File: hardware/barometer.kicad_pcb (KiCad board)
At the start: 2 copper layers, 15 x 25 mm, 24 parts, among them P1 CON-SENSOR2, P2 CONN_01X01, P3 BOOT, U1 XMC1XXX24, U2 LPS22HB, U3 DRILL, U4 DRILL, U5 DRILL, U6 DRILL

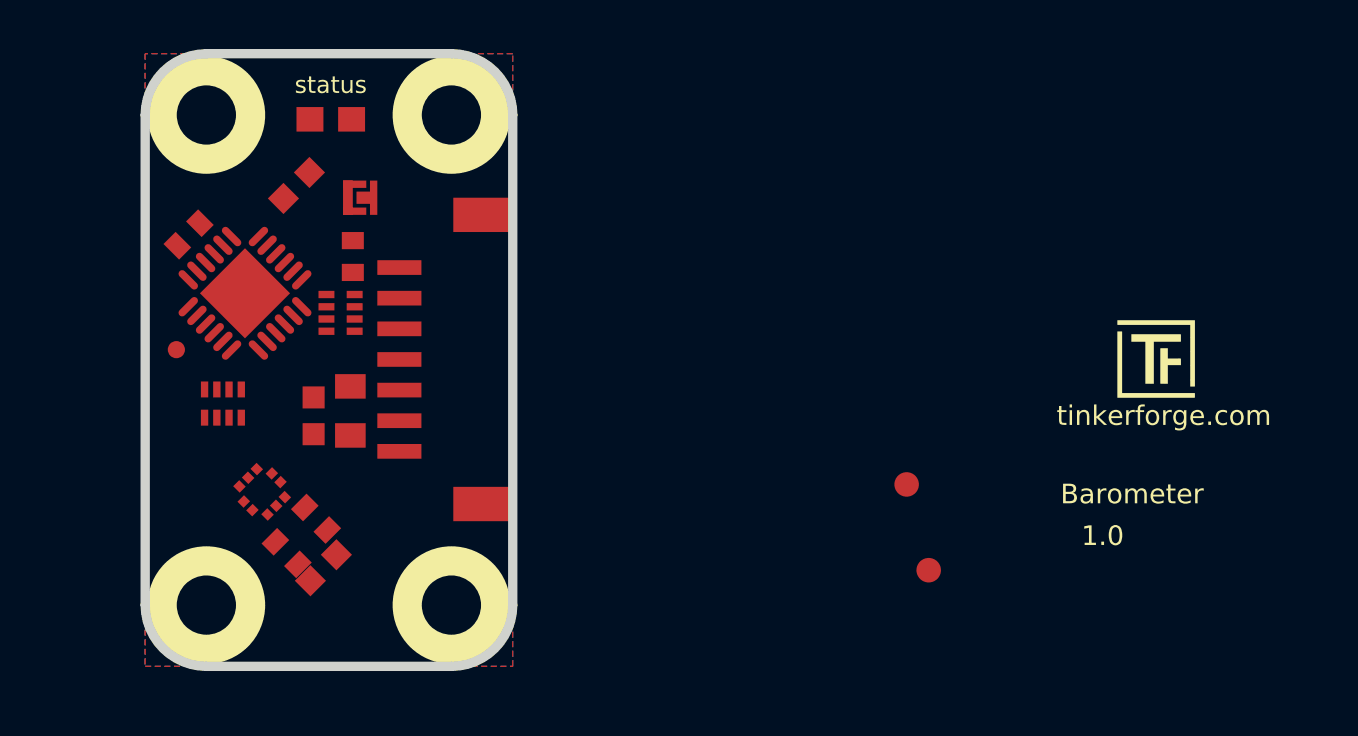
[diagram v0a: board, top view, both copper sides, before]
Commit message: Add early version of PCB
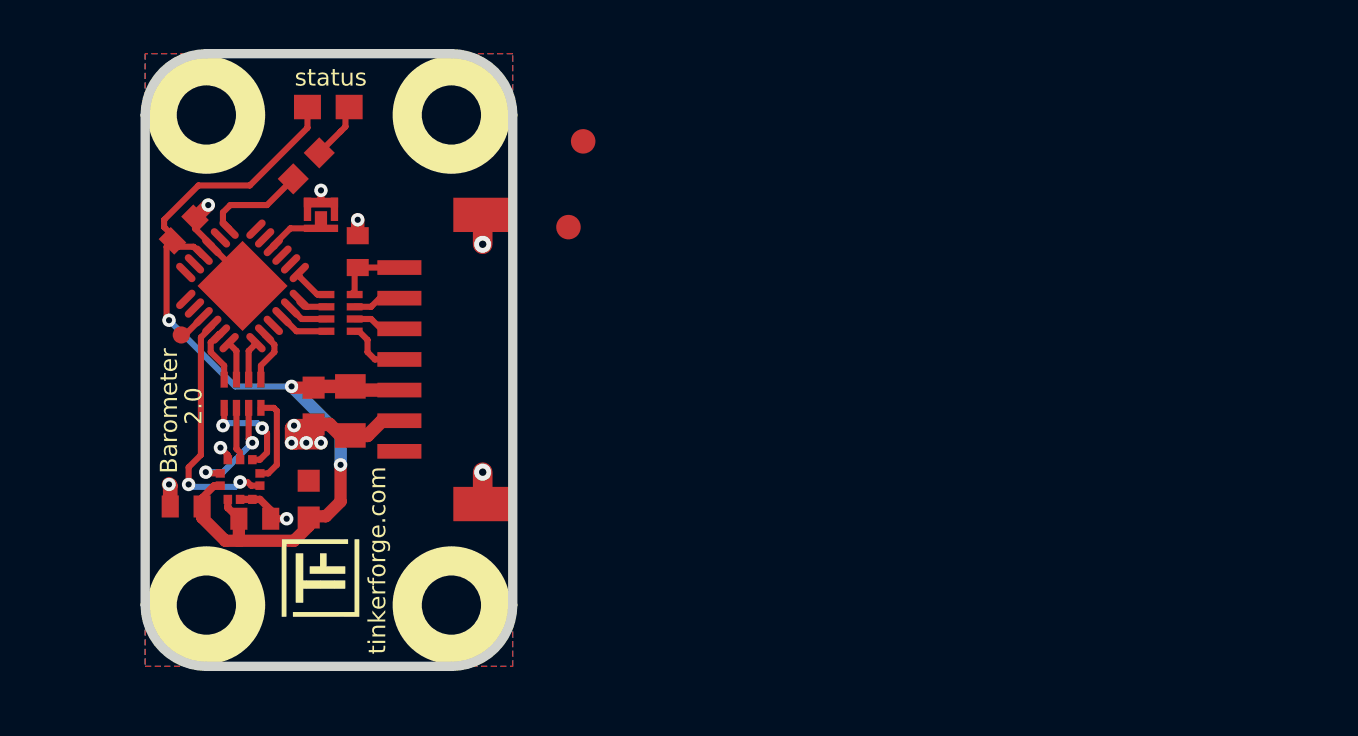
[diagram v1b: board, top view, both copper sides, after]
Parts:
- moved G*** 36.2 mm to (145.9, 113.6), turned to 90 degrees
- moved VAL 24.9 mm to (158.6, 101.3)
- moved Fiducial_Mark 20.3 mm to (157.6, 97.7)
- moved Fiducial_Mark 19.2 mm to (158.2, 94.2)
- moved C5 4.52 mm to (142.0, 109.1), turned to 0 degrees
- moved C7 2.86 mm to (147.0, 108.8), turned to 270 degrees
- moved C6 2.50 mm to (144.8, 109.6), turned to 0 degrees
- moved P3 1.75 mm to (147.5, 97.2), turned to 270 degrees
- moved U2 1.03 mm to (144.2, 108.0), turned to 180 degrees
- moved RP2 0.89 mm to (144.3, 104.5)
- moved R1 0.89 mm to (146.9, 95.2)
- moved P2 0.63 mm to (141.8, 102.1)
- moved D1 0.51 mm to (147.8, 92.8)
- moved C3 0.40 mm to (147.2, 105.0)
- moved U1 0.32 mm to (144.3, 100.1)
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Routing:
- net VCC: track 0.00 -> 41.0 mm, vias 0 -> 3
- net GND: track 0.00 -> 20.1 mm, vias 0 -> 12
- net INT: track 0.00 -> 9.98 mm, vias 0 -> 2
- net M-CLK: track 0.00 -> 4.50 mm, vias 0 -> 2
- net M-MISO: track 0.00 -> 4.27 mm, vias 0 -> 2
- net Net-(R1-Pad1): track 0.00 -> 4.23 mm
- net M-CS: track 0.00 -> 3.81 mm
- net Net-(C1-Pad1): track 0.00 -> 2.96 mm
- net Net-(D1-Pad2): track 0.00 -> 2.87 mm
- net Net-(P1-Pad4): track 0.00 -> 2.59 mm
- net Net-(P3-Pad2): track 0.00 -> 2.33 mm
- net Net-(RP2-Pad8): track 0.00 -> 2.33 mm
- net Net-(RP2-Pad5): track 0.00 -> 2.26 mm
- net M-MOSI: track 0.00 -> 2.18 mm
- net S-CS: track 0.00 -> 2.06 mm
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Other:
- rule trace_min: 0.29972 -> 0.25
- rule via_min_drill: 0.24892 -> 0.24
- rule via_min_size: 0.70104 -> 0.4
- board text added: "2.0"
- board text removed: "1.0"

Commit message: Place CE logo
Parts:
- moved VAL 14.1 mm to (144.7, 99.2)
- moved Fiducial_Mark 1.20 mm to (157.6, 95.2)
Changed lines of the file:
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@@
   (title_block
     (title "Barometric Pressure Bricklet")
-    (date 2017-08-30)
+    (date 2017-09-13)
     (rev 2.0)
     (company "Tinkerforge GmbH")
@@
   )
   (setup
-    (last_trace_width 0.25)
+    (last_trace_width 0.29972)
     (user_trace_width 0.25)
     (user_trace_width 0.29972)
@@
   )
   (module kicad-libraries:CE_5mm (layer Rückseite)
-    (at 158.6 101.3 180)
+    (at 144.675 99.2 180)
     (fp_text reference VAL (at 0 0 180) (layer B.SilkS) hide
       (effects (font (size 0.2 0.2) (thickness 0.05)) (justify mirror))
@@
   )
   (module kicad-libraries:Fiducial_Mark (layer Vorderseite)
-    (at 158.2 94.2)
+    (at 157.625 95.25)
     (path Fiducial_Mark)
     (attr smd)

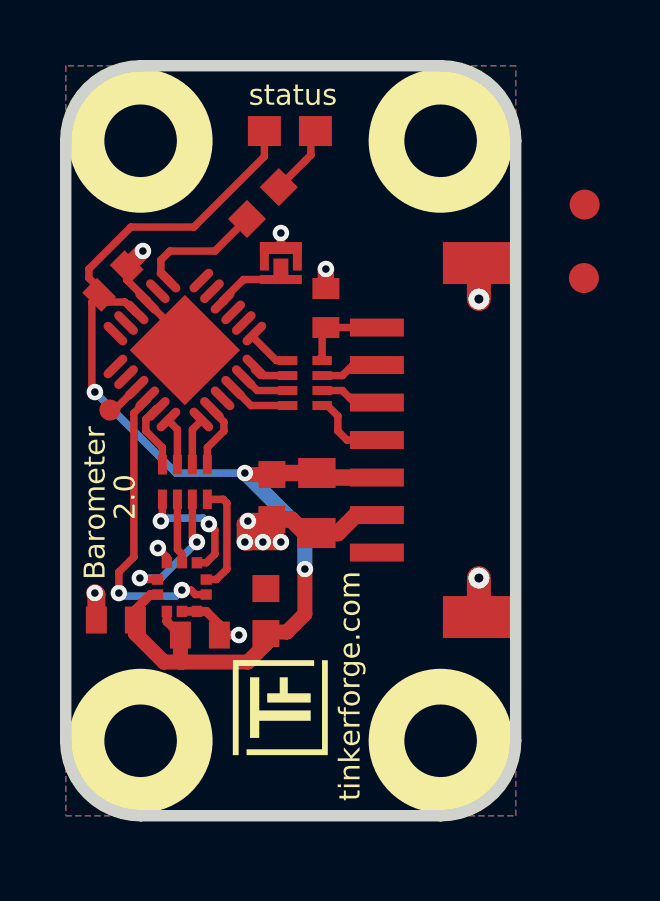
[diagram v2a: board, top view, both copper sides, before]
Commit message: Place fiducials and WEEE logo
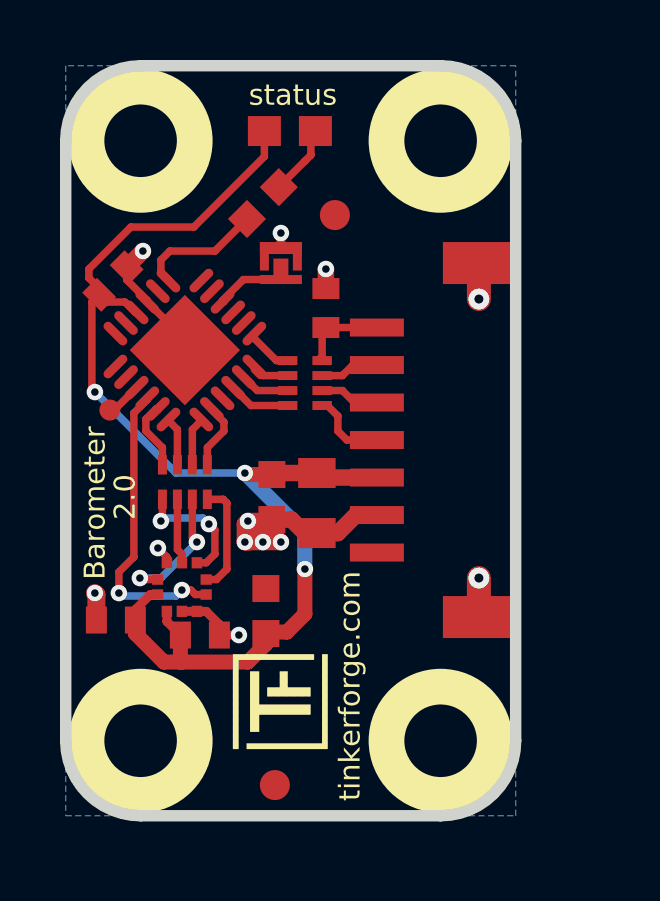
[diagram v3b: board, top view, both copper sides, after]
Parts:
- added VAL: WEEE_7mm, kicad-libraries:WEEE_7mm, B.Cu at (150.8, 102.6)
- moved Fiducial_Mark 19.8 mm to (147.3, 114.6)
- moved Fiducial_Mark 8.33 mm to (149.3, 95.6)
- moved VAL 3.43 mm to (144.2, 102.6)
- moved G*** 0.20 mm to (145.9, 113.4)
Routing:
- removed copper zone on F.Cu, net GND
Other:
- board text added: "Copyright Tinkerforge GmbH 2017. This documentation describes Open Hardware and is licensed under the CERN OHL v. 1.1. You may redistribute and modify this documentation under the terms of the CERN OHL v.1.1. (http://ohwr.org/cernohl). This documentation is distributed WITHOUT ANY EXPRESS OR IMPLIED WARRANTY, INCLUDING OF MERCHANTABILITY, SATISFACTORY QUALITY AND FITNESS FOR A PARTICULAR PURPOSE.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"
- board text removed: "Copyright Tinkerforge GmbH 2011. This documentation describes Open Hardware and is licensed under the CERN OHL v. 1.1. You may redistribute and modify this documentation under the terms of the CERN OHL v.1.1. (http://ohwr.org/cernohl). This documentation is distributed WITHOUT ANY EXPRESS OR IMPLIED WARRANTY, INCLUDING OF MERCHANTABILITY, SATISFACTORY QUALITY AND FITNESS FOR A PARTICULAR PURPOSE.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"

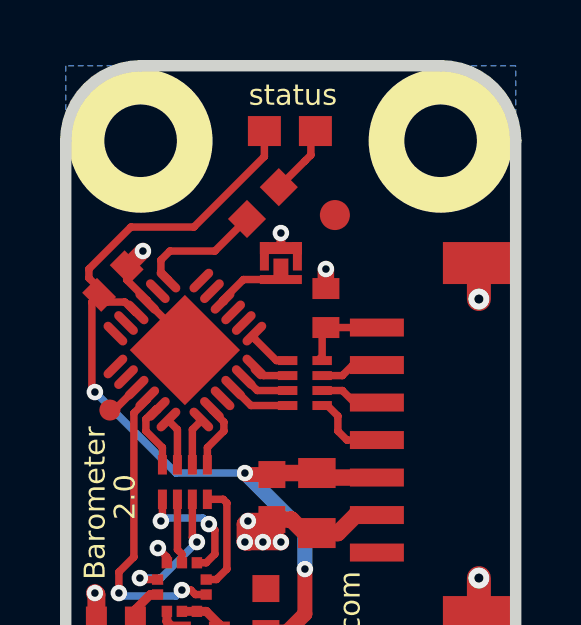
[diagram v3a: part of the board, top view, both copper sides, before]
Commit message: Change RP2, add CoMCU logo
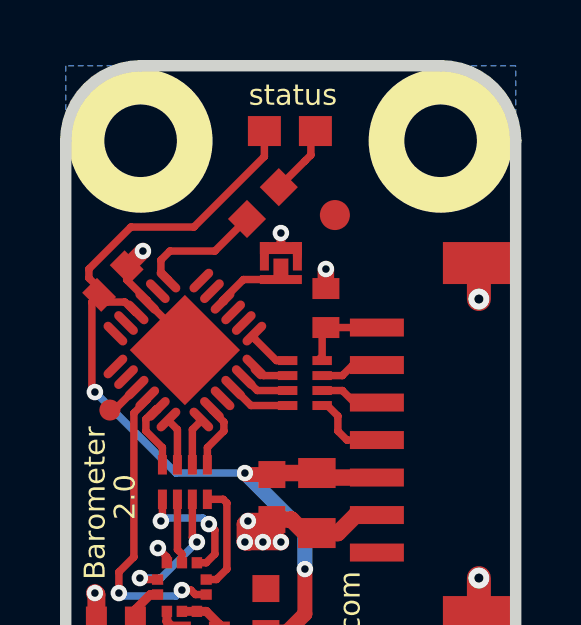
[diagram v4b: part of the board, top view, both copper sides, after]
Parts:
- added G***: LOGO, kicad-libraries:Logo_CoMCU, B.Cu at (150.6, 105.6)
- RP2: value 220 -> 82
- moved VAL 3.29 mm to (149.7, 99.5), turned to 270 degrees
- moved VAL 0.64 mm to (143.8, 103.1), turned to 270 degrees
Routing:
- net GND: track 20.1 -> 25.5 mm

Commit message: Add missing GND via
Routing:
- net GND: track 25.5 -> 26.2 mm, vias 12 -> 13
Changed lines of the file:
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@@
   (general
     (links 53)
-    (no_connects 3)
-    (area 140.136879 90.431619 155.519121 115.813841)
+    (no_connects 2)
+    (area 139.469339 89.769159 284.745862 165.740743)
     (thickness 1.6002)
     (drawings 13)
-    (tracks 204)
+    (tracks 206)
     (zones 0)
     (modules 26)
@@
     (effects (font (size 0.7 0.7) (thickness 0.15)))
   )
+  (segment (start 147 108.05) (end 147 107.3) (width 0.29972) (layer Vorderseite) (net 1))
+  (via (at 147 107.3) (size 0.55) (drill 0.25) (layers Vorderseite Rückseite) (net 1))
   (segment (start 145.219239 100.1) (end 145 100.1) (width 0.29972) (layer Vorderseite) (net 1))
   (segment (start 145 100.1) (end 144.3 100.8) (width 0.29972) (layer Vorderseite) (net 1))

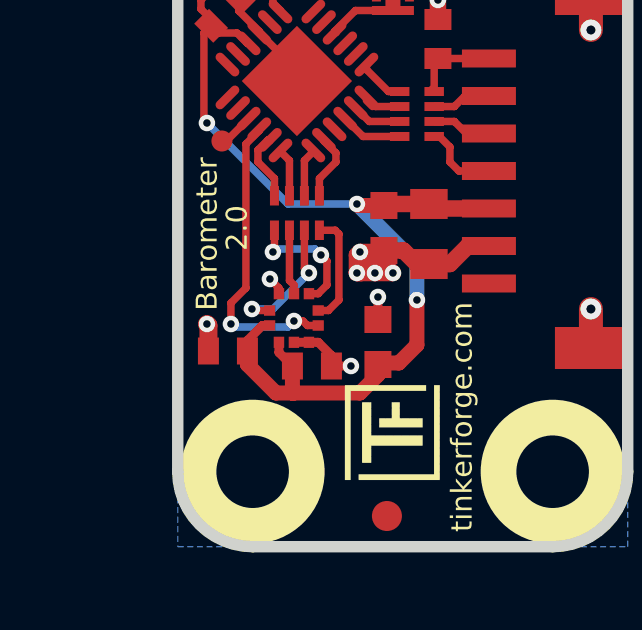
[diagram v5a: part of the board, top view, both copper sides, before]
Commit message: fix footprint, routing not completed
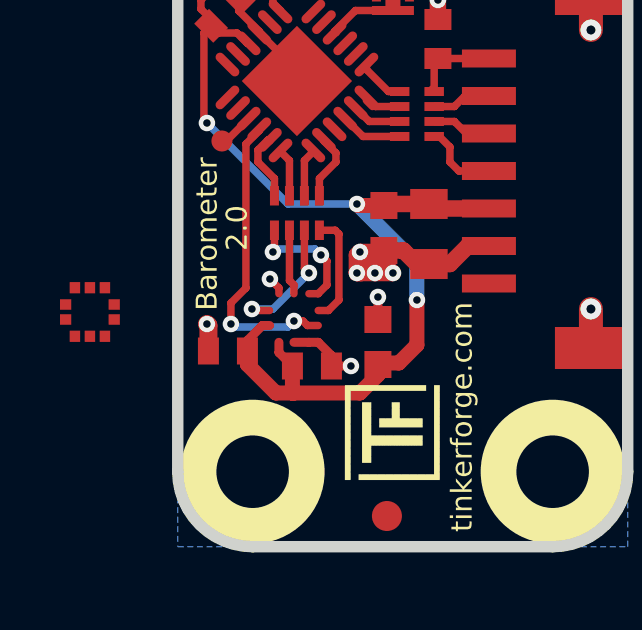
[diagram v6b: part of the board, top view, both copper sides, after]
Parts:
- moved U2 6.80 mm to (137.4, 107.8), turned to 0 degrees
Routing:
- net (no net): track 0.00 -> 0.61 mm, vias 0 -> 1
- net GND: track 26.2 -> 25.6 mm, vias 13 -> 12

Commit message: Fix routing
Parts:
- moved U2 6.63 mm to (144.0, 107.2)
- moved C6 0.82 mm to (145.2, 108.9)
- moved P2 0.22 mm to (141.6, 102.2)
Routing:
- net INT: track 9.98 -> 7.01 mm, vias 2 -> 0
- net M-MISO: track 4.27 -> 1.34 mm, vias 2 -> 0
- net M-CS: track 3.81 -> 5.25 mm, vias 0 -> 2
- net M-MOSI: track 2.18 -> 1.34 mm
- net VCC: track 41.0 -> 41.8 mm
- net (no net): track 0.61 -> 0.00 mm, vias 1 -> 0
- net GND: track 25.6 -> 25.8 mm, vias 12 -> 14
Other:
- rule trace_min: 0.25 -> 0.19

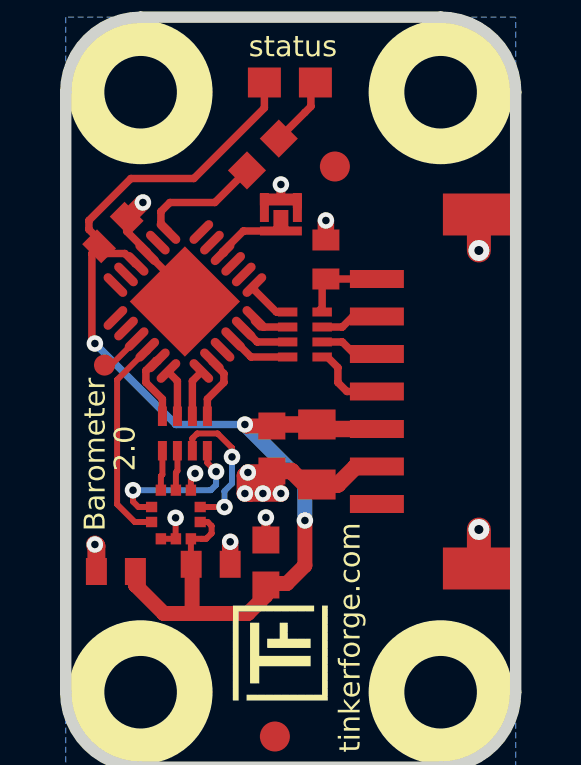
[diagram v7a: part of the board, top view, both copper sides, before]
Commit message: change 0402E footprints to 0402F
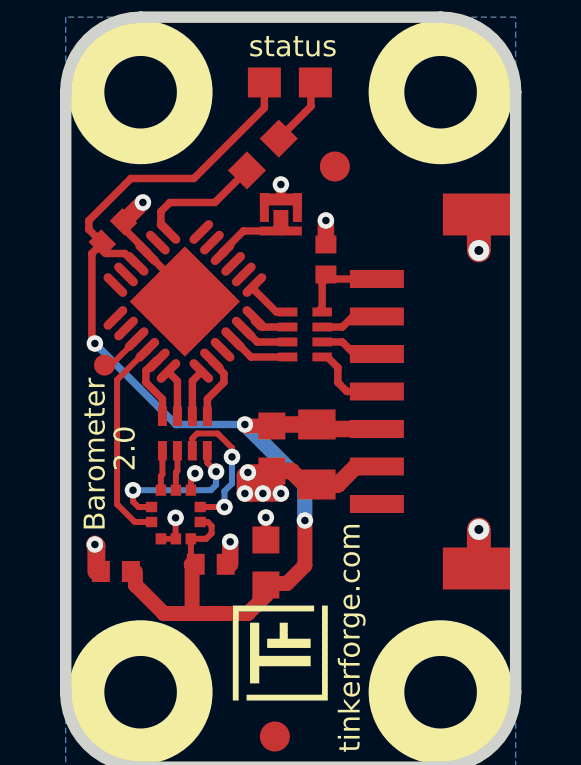
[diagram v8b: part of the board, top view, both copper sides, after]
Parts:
- C1, C4, C5, C6: footprint kicad-libraries:C0402E -> kicad-libraries:C0402F
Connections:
- P1 pad 1: Net-(P1-Pad1) -> (no net)
- U1 pad 11: Net-(U1-Pad11) -> (no net)
- U1 pad 12: Net-(U1-Pad12) -> (no net)
- U1 pad 13: Net-(U1-Pad13) -> (no net)
- U1 pad 14: Net-(U1-Pad14) -> (no net)
- U1 pad 2: Net-(U1-Pad2) -> (no net)
- U1 pad 21: Net-(U1-Pad21) -> (no net)
- U1 pad 3: Net-(U1-Pad3) -> (no net)
- U1 pad 5: Net-(U1-Pad5) -> (no net)
- U1 pad 6: Net-(U1-Pad6) -> (no net)
- U1 pad 8: Net-(U1-Pad8) -> (no net)
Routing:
- net GND: track 25.8 -> 27.1 mm
